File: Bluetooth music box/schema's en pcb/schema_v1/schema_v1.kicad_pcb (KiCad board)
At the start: 4 copper layers, 141 x 87.6 mm, 145 parts, among them J1 Pickit aansluiting, J2 USB_B_Micro, SW1 SW_Push, SW3 SW_Push, SW4 SW_Push, SW5 SW_Push, SW6 SW_Push, SW7 SW_Push, SW9 Switch, U1 LTC2063, U10 SN74LVC1T45DBV, U11 tpa3140, U12 LTC4001, U14 TPS563200, U2 pic18f27k40, U5 FT232RL, U6 LM1117-3.3, U8 OVC3860_EDR, U9 Spi_header

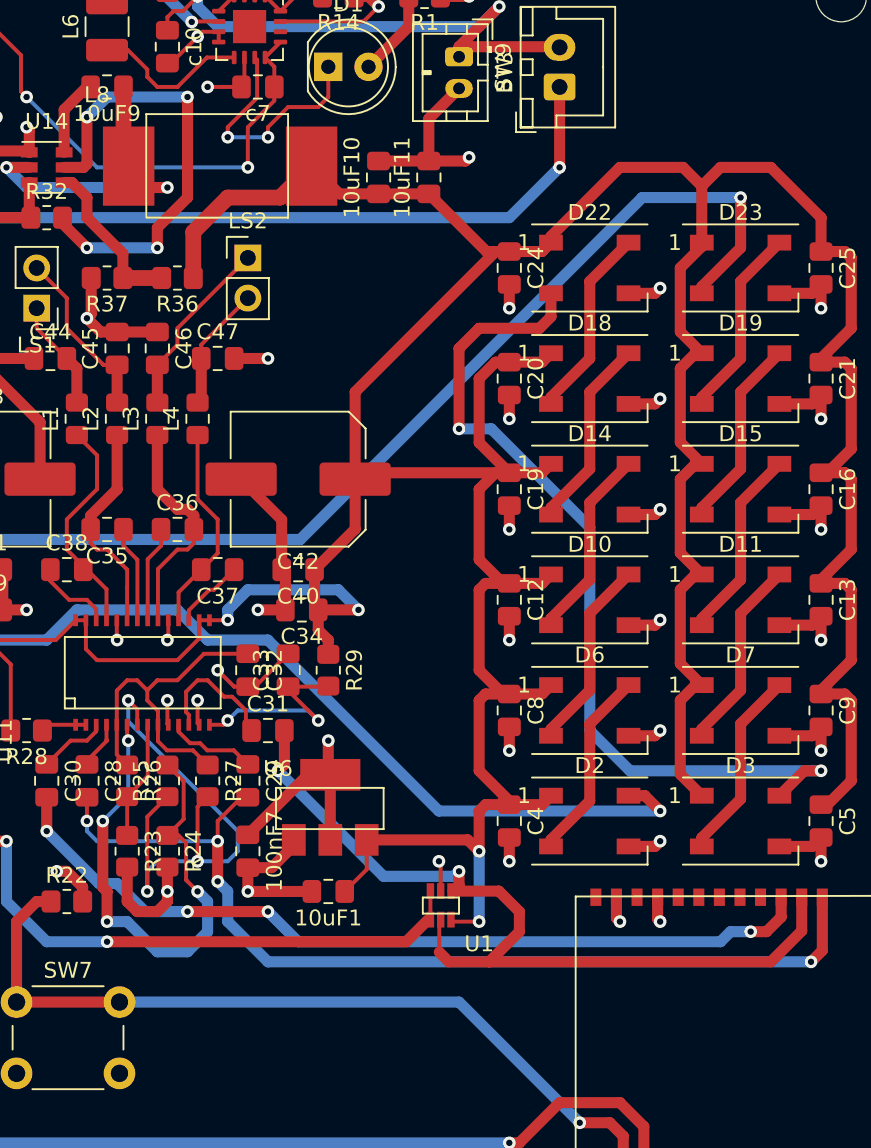
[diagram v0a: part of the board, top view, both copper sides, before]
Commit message: aanpassing schema en pcb
oplossing voor audiosignalen
in excel nog enkele links toegevoegd
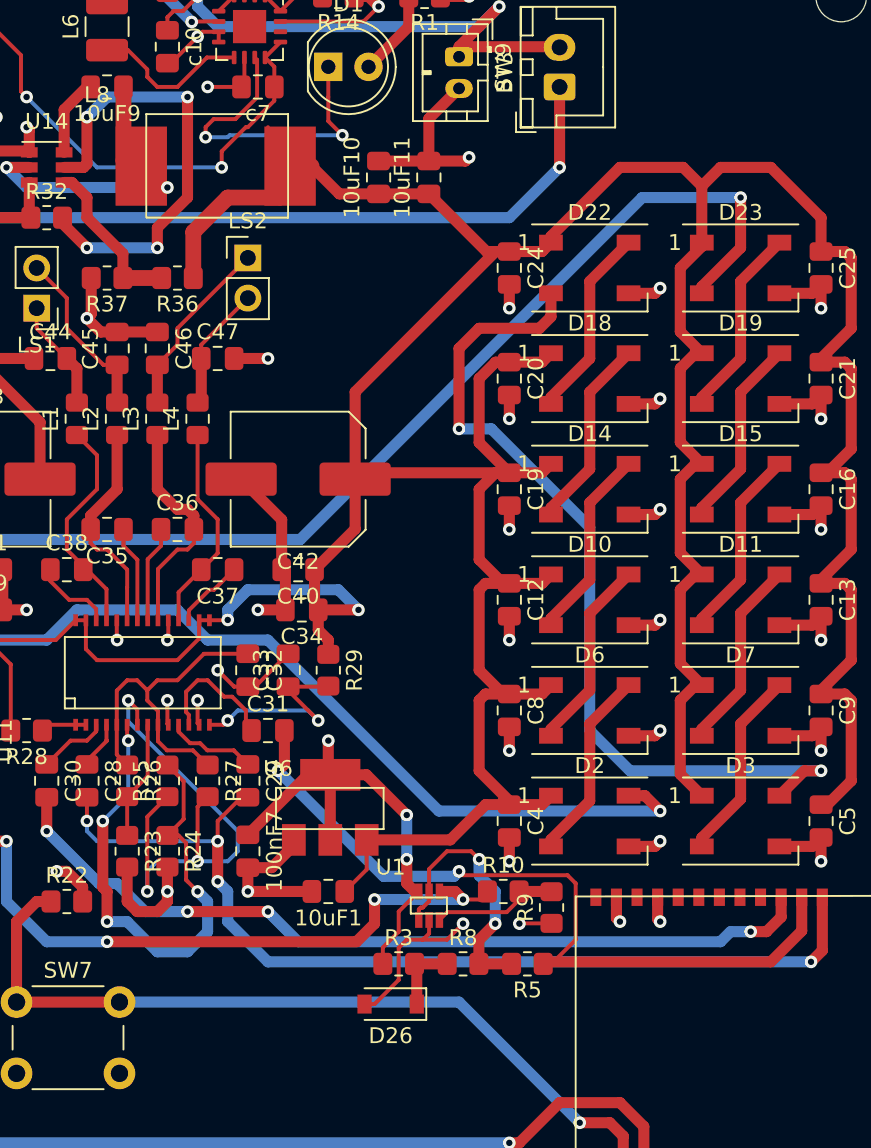
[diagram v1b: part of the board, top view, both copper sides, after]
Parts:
- added D26: D_Zener, Diode_SMD:D_SOD-123, F.Cu at (184.9, 116.3)
- added R10: 10k, Resistor_SMD:R_0805_2012Metric_Pad1.20x1.40mm_HandSolder, F.Cu at (192.0, 109.2)
- added R3: 10k, Resistor_SMD:R_0805_2012Metric_Pad1.20x1.40mm_HandSolder, F.Cu at (185.4, 113.8)
- added R5: 100k, Resistor_SMD:R_0805_2012Metric_Pad1.20x1.40mm_HandSolder, F.Cu at (193.5, 113.8)
- added R8: 100k, Resistor_SMD:R_0805_2012Metric_Pad1.20x1.40mm_HandSolder, F.Cu at (189.5, 113.8)
- added R9: 100k, Resistor_SMD:R_0805_2012Metric_Pad1.20x1.40mm_HandSolder, F.Cu at (195.1, 110.2)
- moved U1 8.08 mm to (184.9, 107.2), turned to 0 degrees
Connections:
- U1 pad 1: VoL_Measure -> Net-(R5-Pad2)
- U1 pad 3: Vol_spkr -> Net-(R10-Pad2)
- U1 pad 5: VoL_Measure -> Net-(R5-Pad2)
- U1 pad 6: +5V -> +3V3
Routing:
- net Net-(R5-Pad2): track 0.00 -> 16.9 mm, vias 0 -> 2
- net +3V3: track 40.4 -> 57.0 mm, vias 12 -> 14
- net GND: track 257.9 -> 269.1 mm, vias 74 -> 75
- net Net-(R10-Pad2): track 0.00 -> 8.14 mm
- net +5V: track 563.3 -> 555.4 mm, vias 8 -> 6
- net Vol_spkr: track 96.9 -> 102.0 mm, vias 4 -> 6
- net Net-(D1-Pad1): track 15.5 -> 20.6 mm
- net VoL_Measure: track 55.3 -> 50.3 mm
- net Net-(D26-Pad1): track 0.00 -> 4.66 mm
- net Vusb: track 34.1 -> 33.3 mm

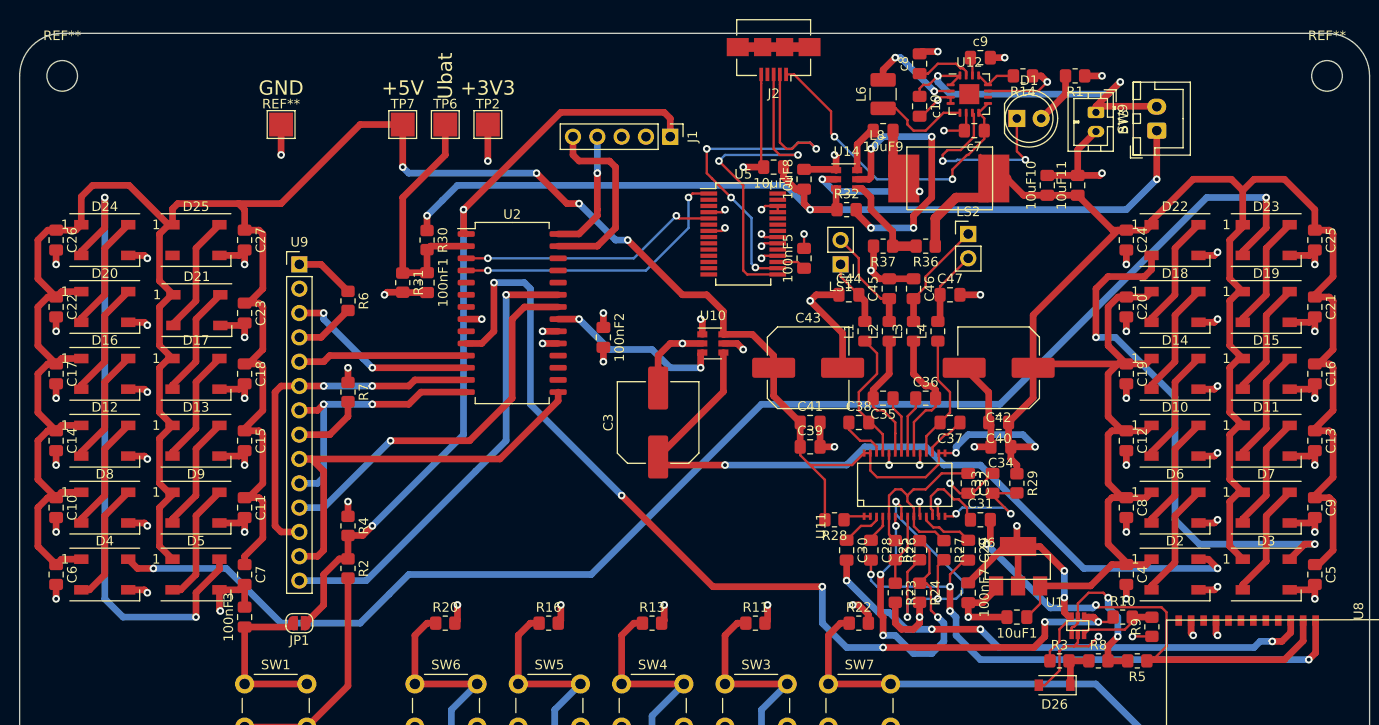
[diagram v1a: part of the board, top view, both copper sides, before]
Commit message: eerste code test
nog niet getest, enkel geschreven
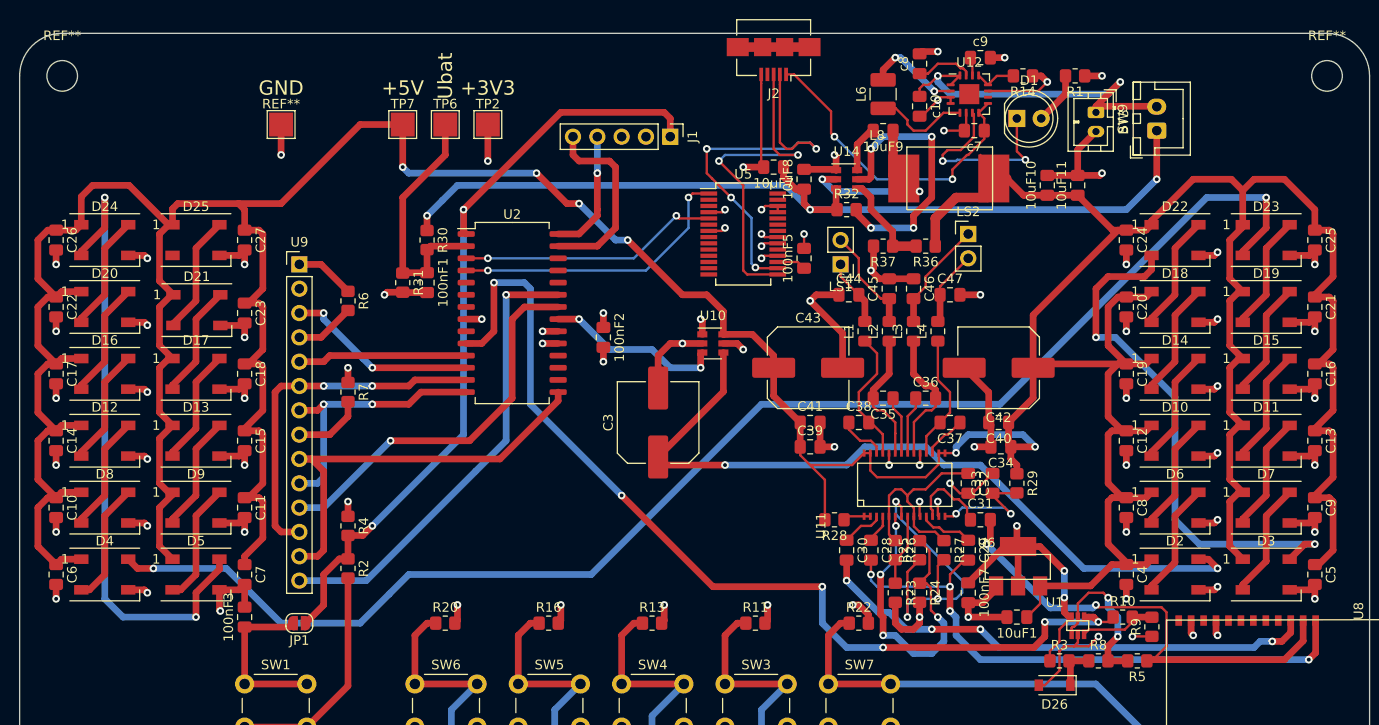
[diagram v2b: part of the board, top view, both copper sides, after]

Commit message: Nieuwe start
Nieuw schema (andere µC, BT-module, dc/dc, verschillversterkers)
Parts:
- removed 100nF1, 100nF2, 100nF3, 100nF5, 100nF7, 10uF1, 10uF7, 10uF8: C, Capacitor_SMD:C_0805_2012Metric_Pad1.18x1.45mm_HandSolder
- removed 10uF10, 10uF11: 22µF, Capacitor_SMD:C_0805_2012Metric_Pad1.18x1.45mm_HandSolder
- removed 10uF9: 0.1µF, Capacitor_SMD:C_0805_2012Metric_Pad1.18x1.45mm_HandSolder
- removed L8: 2.2uH, Robbe_modules:L_tps563200
- removed R20, R22, R32, R37: 10k, Resistor_SMD:R_0805_2012Metric_Pad1.20x1.40mm_HandSolder
- removed R36: 56k, Resistor_SMD:R_0805_2012Metric_Pad1.20x1.40mm_HandSolder
- removed REF**: TestPoint_GND, TestPoint:TestPoint_Pad_2.5x2.5mm
- removed REF** (x4): MountingHole_3.2mm_M3, MountingHole:MountingHole_3.2mm_M3
- removed SW7: SW_Push, Button_Switch_THT:SW_PUSH_6mm_H7.3mm
- removed TP2, TP7: TestPoint, TestPoint:TestPoint_Pad_2.5x2.5mm
- removed U10: SN74LVC1T45DBV, Package_TO_SOT_SMD:SOT-23-6
- removed U14: TPS563200, Package_TO_SOT_SMD:SOT-23-6
- removed U8: OVC3860_EDR, Robbe_modules:OVC3860_EDR
- added C1: 100nF, Capacitor_SMD:C_0805_2012Metric_Pad1.18x1.45mm_HandSolder, F.Cu at (106.9, 62.7)
- added C2: 10uF, Capacitor_SMD:C_0805_2012Metric_Pad1.18x1.45mm_HandSolder, F.Cu at (111.7, 62.7)
- added C48: 100nF, Capacitor_SMD:C_0805_2012Metric_Pad1.18x1.45mm_HandSolder, F.Cu at (106.9, 65.7)
- added C49: 100nF, Capacitor_SMD:C_0805_2012Metric_Pad1.18x1.45mm_HandSolder, F.Cu at (88.3, 70.0)
- added C50: 10uF, Capacitor_SMD:C_0805_2012Metric_Pad1.18x1.45mm_HandSolder, F.Cu at (169.7, 66.4)
- added C51: 100nF, Capacitor_SMD:C_0805_2012Metric_Pad1.18x1.45mm_HandSolder, F.Cu at (216.8, 86.1)
- added C52: 100nF, Capacitor_SMD:C_0805_2012Metric_Pad1.18x1.45mm_HandSolder, F.Cu at (205.6, 97.5)
- added C53: 100nF, Capacitor_SMD:C_0805_2012Metric_Pad1.18x1.45mm_HandSolder, F.Cu at (212.2, 93.3)
- added C54: 100nF, Capacitor_SMD:C_0805_2012Metric_Pad1.18x1.45mm_HandSolder, F.Cu at (200.8, 97.5)
- added C55: 100nF, Capacitor_SMD:C_0805_2012Metric_Pad1.18x1.45mm_HandSolder, F.Cu at (212.2, 96.3)
- added C56: 10nF, Capacitor_SMD:C_0805_2012Metric_Pad1.18x1.45mm_HandSolder, F.Cu at (216.8, 89.1)
- added C57: 100nF, Capacitor_SMD:C_0805_2012Metric_Pad1.18x1.45mm_HandSolder, F.Cu at (232.4, 60.4)
- added D27: RED, LED_SMD:LED_0603_1608Metric_Pad1.05x0.95mm_HandSolder, F.Cu at (174.3, 64.0)
- added D28: D_Schottky, Diode_SMD:D_SOD-128, F.Cu at (209.3, 72.0)
- added D29: RED, LED_SMD:LED_0603_1608Metric_Pad1.05x0.95mm_HandSolder, F.Cu at (232.8, 72.2)
- added J3: Conn_01x05_Male, Connector_PinSocket_2.54mm:PinSocket_1x05_P2.54mm_Vertical, F.Cu at (196.1, 86.9)
- added JP2: SolderJumper, Jumper:SolderJumper-2_P1.3mm_Open_TrianglePad1.0x1.5mm, F.Cu at (183.3, 57.0)
- added JP3: SolderJumper, Jumper:SolderJumper-2_P1.3mm_Open_TrianglePad1.0x1.5mm, F.Cu at (178.8, 61.6)
- added JP4: SolderJumper, Jumper:SolderJumper-2_P1.3mm_Open_TrianglePad1.0x1.5mm, F.Cu at (169.5, 72.6)
- added JP5: Jumper, Connector_PinSocket_2.54mm:PinSocket_1x02_P2.54mm_Vertical, F.Cu at (174.2, 55.0)
- added JP6: Jumper, Connector_PinSocket_2.54mm:PinSocket_1x02_P2.54mm_Vertical, F.Cu at (178.8, 55.0)
- added JP7: SolderJumper, Jumper:SolderJumper-2_P1.3mm_Open_TrianglePad1.0x1.5mm, F.Cu at (237.5, 69.6)
- added JP8: Jumper, Connector_PinSocket_2.54mm:PinSocket_1x02_P2.54mm_Vertical, F.Cu at (212.1, 86.9)
- added L5: 2.2uH, Robbe_modules:L_tps563200, F.Cu at (206.4, 53.4)
- added R12: 100, Resistor_SMD:R_0805_2012Metric_Pad1.20x1.40mm_HandSolder, F.Cu at (169.7, 69.4)
- added R15: 562K, Resistor_SMD:R_0805_2012Metric_Pad1.20x1.40mm_HandSolder, F.Cu at (242.0, 60.1)
- added R17: 100, Resistor_SMD:R_0805_2012Metric_Pad1.20x1.40mm_HandSolder, F.Cu at (228.2, 69.4)
- added R18: 10K, Resistor_SMD:R_0805_2012Metric_Pad1.20x1.40mm_HandSolder, F.Cu at (216.9, 92.1)
- added SW2: SW_Push, Button_Switch_THT:SW_PUSH_6mm_H7.3mm, F.Cu at (170.3, 122.9)
- added U3: RN52, Robbe_modules:RN52, F.Cu at (152.5, 79.1)
- added U4: STM32L443CCTx, Package_QFP:LQFP-48_7x7mm_P0.5mm, F.Cu at (204.1, 90.3)
- added U7: TLV61048, Package_TO_SOT_SMD:SOT-23-6_Handsoldering, F.Cu at (225.5, 61.5)
- added c1: 1uF, Capacitor_SMD:C_0805_2012Metric_Pad1.18x1.45mm_HandSolder, F.Cu at (229.8, 66.5)
- added c2: 10µF, Capacitor_SMD:C_0805_2012Metric_Pad1.18x1.45mm_HandSolder, F.Cu at (237.2, 60.4)
- D26: value D_Zener -> BLUE; footprint Diode_SMD:D_SOD-123 -> LED_SMD:LED_0603_1608Metric_Pad1.05x0.95mm_HandSolder
- J1: value Pickit aansluiting -> Conn_01x04; footprint Connector_PinHeader_2.54mm:PinHeader_1x05_P2.54mm_Vertical -> Connector_PinSocket_2.54mm:PinSocket_1x04_P2.54mm_Vertical
- JP1: footprint Jumper:SolderJumper-2_P1.3mm_Open_RoundedPad1.0x1.5mm -> Jumper:SolderJumper-2_P1.3mm_Open_TrianglePad1.0x1.5mm
- R10, R11, R4: value 10k -> 220K
- R13: value 10k -> 100
- R16: value 10k -> 107K
- R2: value 100 -> 100K
- R3: value 10k -> 100K
- R5: value 100k -> 220K
- R8, R9: value 100k -> 100K
- U1: value LTC2063 -> TL072; footprint Robbe_modules:LTC2063 -> Package_SO:SO-8_3.9x4.9mm_P1.27mm
- U2: value pic18f27k40 -> SN74LVC1T45DBV; footprint Package_SO:SOIC-28W_7.5x18.7mm_P1.27mm -> Package_TO_SOT_SMD:SOT-23-6
- moved D7 122.5 mm to (85.5, 113.1)
- moved R30 120.0 mm to (238.7, 57.1), turned to 0 degrees
- moved TP6 119.2 mm to (240.3, 64.2)
- moved R31 116.2 mm to (233.0, 69.4), turned to 0 degrees
- moved D10 115.7 mm to (85.5, 119.7)
- moved D11 115.3 mm to (93.9, 113.1)
- moved R16 113.5 mm to (235.6, 63.4)
- moved D22 109.0 mm to (102.3, 123.1)
- moved R5 107.7 mm to (93.1, 75.0), turned to 0 degrees
- moved D23 107.0 mm to (110.8, 116.5)
- moved R10 105.6 mm to (93.1, 72.1)
- moved R9 105.2 mm to (97.9, 69.9), turned to 0 degrees
- moved D18 103.1 mm to (102.3, 116.5)
- moved R3 102.5 mm to (88.3, 80.9)
- moved C21 101.7 mm to (122.2, 124.3), turned to 0 degrees
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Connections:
- C28 pad 2: /Class d amplifier/Agnd -> /L-
- C29 pad 2: /Class d amplifier/Agnd -> /R-
- C3 pad 1: DataLeds -> +5V
- C30 pad 2: /Class d amplifier/Aleft -> /L+
- C31 pad 2: VoL_Measure -> /R+
- D2 pad 4: DataLeds -> /LEDS/FirstLED
- D26 pad 2: GND -> +3V3
- J1 pad 1: Reset -> Net-(J1-Pad1)
- J1 pad 2: +3V3 -> Net-(J1-Pad2)
- J1 pad 3: GND -> Net-(J1-Pad3)
- J1 pad 4: PGD -> Net-(J1-Pad4)
- JP1 pad 1: Reset -> RTS_BT
- JP1 pad 2: Net-(100nF3-Pad1) -> Net-(J1-Pad1)
- R10 pad 1: Vol_spkr -> GND
- R11 pad 1: vol+ -> /R_SE
- R11 pad 2: GND -> Net-(R11-Pad2)
- R13 pad 1: vol- -> Net-(R13-Pad1)
- R13 pad 2: GND -> Net-(D27-Pad1)
- R16 pad 1: next -> Net-(R15-Pad2)
- R2 pad 1: Reset -> Net-(R2-Pad1)
- R2 pad 2: Net-(R2-Pad2) -> /L+
- R3 pad 1: +3V3 -> Net-(R3-Pad1)
- R3 pad 2: Net-(D26-Pad1) -> /L-
- R4 pad 1: +3V3 -> GND
- R4 pad 2: Reset -> Net-(R3-Pad1)
- R5 pad 1: VoL_Measure -> /L_SE
- R5 pad 2: Net-(R5-Pad2) -> Net-(R2-Pad1)
- R6 pad 2: LCS_rst -> LCD_rst
- R8 pad 1: Net-(D26-Pad1) -> Net-(R11-Pad2)
- R8 pad 2: Net-(R5-Pad2) -> /R+
- R9 pad 1: GND -> Net-(R10-Pad2)
- R9 pad 2: Net-(R10-Pad2) -> /R-
- SW1 pad 1: Net-(100nF3-Pad1) -> GND
- SW1 pad 2: Net-(R2-Pad2) -> Reset
- SW3 pad 1: vol+ -> GND
- SW3 pad 2: +3V3 -> vol-
- SW4 pad 1: vol- -> GND
- SW4 pad 2: +3V3 -> next
- SW5 pad 1: next -> GND
- SW5 pad 2: +3V3 -> prev
- SW6 pad 1: prev -> GND
- SW6 pad 2: +3V3 -> pp
- U1 pad 1: Net-(R5-Pad2) -> /L_SE
- U1 pad 2: GND -> Net-(R3-Pad1)
- U1 pad 3: Net-(R10-Pad2) -> Net-(R2-Pad1)
- U1 pad 4: Vol_spkr -> GND
- U1 pad 5: Net-(R5-Pad2) -> Net-(R11-Pad2)
- U1 pad 6: +3V3 -> Net-(R10-Pad2)
- U2 pad 1: Reset -> +3V3
- U2 pad 2: BAT_ADC -> GND
- U2 pad 3: TX -> /LEDS/D_LEDS
- U2 pad 4: RX -> /LEDS/FirstLED
- U2 pad 5: RA3 -> +3V3
- U2 pad 6: Net-(U2-Pad6) -> +5V
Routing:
- net +5V: track 555.4 -> 0.00 mm, vias 6 -> 0
- net GND: track 269.1 -> 0.00 mm, vias 75 -> 0
- net Net-(D23-Pad2): track 147.1 -> 0.00 mm, vias 2 -> 0
- net prev: track 120.2 -> 0.00 mm, vias 1 -> 0
- net next: track 103.9 -> 0.00 mm, vias 1 -> 0
- net Vol_spkr: track 102.0 -> 0.00 mm, vias 6 -> 0
- net Vbat: track 98.2 -> 0.00 mm, vias 3 -> 0
- net vol-: track 88.0 -> 0.00 mm, vias 1 -> 0
- net Reset: track 82.1 -> 0.00 mm, vias 2 -> 0
- net DataLeds: track 80.9 -> 0.00 mm, vias 2 -> 0
- net vol+: track 74.3 -> 0.00 mm, vias 1 -> 0
- net Net-(D24-Pad2): track 66.3 -> 0.00 mm, vias 2 -> 0
- net /Class d amplifier/Agnd: track 62.1 -> 0.00 mm, vias 4 -> 0
- net +3V3: track 57.0 -> 0.00 mm, vias 14 -> 0
- net Net-(D22-Pad2): track 55.8 -> 0.00 mm, vias 2 -> 0
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- removed copper zone on In1.Cu, net +3V3
- removed copper zone on In2.Cu, net GND
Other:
- board size 141 x 87.6 mm -> 175.8 x 90.9 mm
- board text removed: "+3V3"
- board text removed: "+5V"
- board text removed: "GND"
- board text removed: "Robbe Janssens /// 2020-2021 /// Practice Enterprise 2 /// 2EH1"
- board text removed: "Ubat"

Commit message: Werken aan positionering componenten op pcb
kleine aanpassingen op schema (zoals verbinding leds - µc)
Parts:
- R1: value 10k -> 1k
- moved D29 172.4 mm to (60.5, 75.2), turned to 270 degrees
- moved R17 168.1 mm to (60.5, 79.2), turned to 270 degrees
- moved JP7 143.2 mm to (96.0, 91.4), turned to 270 degrees
- moved R15 142.9 mm to (102.6, 91.4)
- moved D26 139.5 mm to (64.5, 127.0), turned to 270 degrees
- moved R30 138.8 mm to (102.1, 81.8), turned to 270 degrees
- moved c2 138.6 mm to (102.6, 93.5)
- moved C28 135.8 mm to (51.3, 112.8), turned to 270 degrees
- moved R28 135.1 mm to (51.3, 106.7), turned to 90 degrees
- moved C57 134.6 mm to (99.6, 81.8), turned to 90 degrees
- moved R16 132.8 mm to (105.7, 90.9), turned to 90 degrees
- moved C35 130.5 mm to (55.9, 98.0), turned to 180 degrees
- moved L1 129.9 mm to (57.4, 94.5), turned to 90 degrees
- moved R31 128.9 mm to (104.6, 81.8), turned to 90 degrees
- moved D27 128.3 mm to (62.5, 127.0), turned to 270 degrees
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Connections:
- net /LEDS/D_LEDS renamed DataLeds
- net Net-(U4-Pad26) renamed /STM32G0/LedData
- U9 pad 4: LCS_rst -> LCD_rst
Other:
- board size 175.8 x 90.9 mm -> 262.6 x 99.6 mm

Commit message: pcb componenten goed gepositioneerd (pcb_v3)
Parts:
- moved C56 123.7 mm to (146.8, 72.1), turned to 180 degrees
- moved C51 111.8 mm to (152.9, 73.2), turned to 90 degrees
- moved C55 109.3 mm to (154.9, 86.9), turned to 270 degrees
- moved TP6 108.2 mm to (166.1, 57.4)
- moved C52 107.7 mm to (145.8, 86.9), turned to 270 degrees
- moved C27 106.1 mm to (83.8, 62.5), turned to 270 degrees
- moved C18 106.1 mm to (83.8, 69.6), turned to 270 degrees
- moved C17 103.7 mm to (83.8, 90.9), turned to 270 degrees
- moved C54 103.1 mm to (146.8, 74.2), turned to 180 degrees
- moved C53 100.9 mm to (158.5, 77.7)
- moved C11 96.1 mm to (83.8, 76.7), turned to 270 degrees
- moved C15 96.0 mm to (94.5, 69.6), turned to 270 degrees
- moved C22 93.7 mm to (94.5, 83.8), turned to 270 degrees
- moved C7 93.4 mm to (94.5, 76.7), turned to 270 degrees
- moved C26 92.9 mm to (83.8, 83.8), turned to 270 degrees
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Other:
- board size 262.6 x 99.6 mm -> 137.7 x 65.5 mm

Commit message: Tracks tekenen op pcb
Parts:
- moved C44 0.51 mm to (124.0, 68.6)
- moved C45 0.51 mm to (124.0, 66.0)
- turned R13 to 180 degrees
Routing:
- net +5V: track 0.00 -> 375.5 mm, vias 0 -> 4
- net Reset: track 0.00 -> 184.8 mm, vias 0 -> 6
- net /L-: track 0.00 -> 171.8 mm, vias 0 -> 4
- net Net-(D23-Pad2): track 0.00 -> 163.7 mm, vias 0 -> 2
- net /L+: track 0.00 -> 153.0 mm, vias 0 -> 2
- net Net-(C37-Pad2): track 0.00 -> 149.8 mm, vias 0 -> 6
- net /R+: track 0.00 -> 117.6 mm, vias 0 -> 6
- net GND: track 0.00 -> 104.3 mm
- net LCD_SDI: track 0.00 -> 64.3 mm, vias 0 -> 1
- net LCD_SDO: track 0.00 -> 60.2 mm, vias 0 -> 2
- net /R-: track 0.00 -> 59.3 mm, vias 0 -> 1
- net EVENT: track 0.00 -> 56.1 mm, vias 0 -> 2
- net LCD_SCK: track 0.00 -> 55.7 mm, vias 0 -> 2
- net pp: track 0.00 -> 55.4 mm, vias 0 -> 1
- net LCD_CS: track 0.00 -> 54.1 mm, vias 0 -> 1
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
